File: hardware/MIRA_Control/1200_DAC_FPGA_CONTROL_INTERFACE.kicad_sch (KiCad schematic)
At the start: 16 parts, among them U500 XC7A200T-2FBG484I

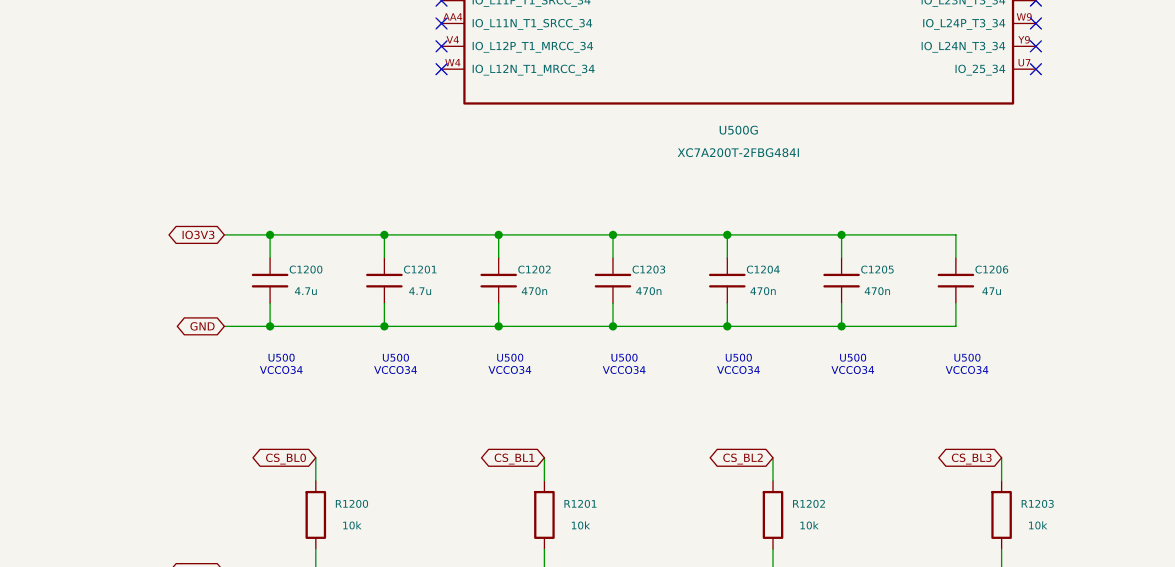
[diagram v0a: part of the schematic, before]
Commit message: Add high-load schematic candidate with CORE sense and revised N15 supply
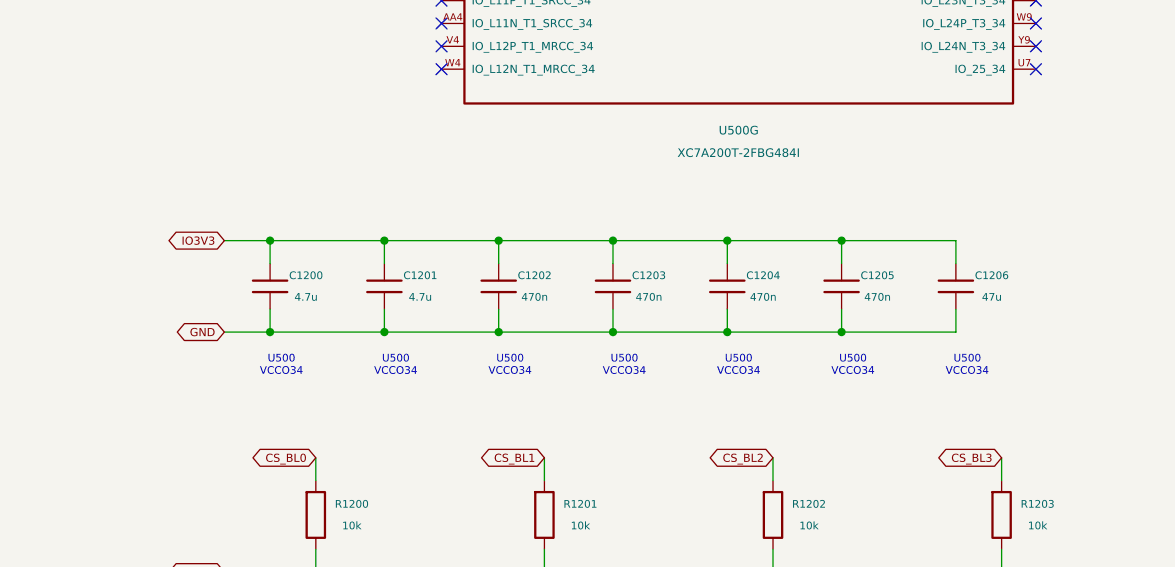
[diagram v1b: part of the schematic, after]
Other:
- moved on the sheet: C1200, C1201, C1202, C1203, C1204, C1205, C1206
